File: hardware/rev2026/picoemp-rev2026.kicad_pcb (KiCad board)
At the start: 2 copper layers, 40 x 130 mm, 53 parts, among them J1 EDGE-SMA, J2 1x2_Pin_Header, J3 MKDS 1,5/2-5.08, J4 EDGE-SMA, P1 Header 7, P2 Header 2, P3 Header 4, Q1 LDA111STR, Q2 RGT16BM65DTL, Q3 AO3422, Q4 AO3422, SW1 KSC741J LFS, SW2 KSC741J LFS, SW3 TL3301AF160QJ, T1 ATB322524, T2 ATB322524, U1 SC0915, U2 74LVC1G17

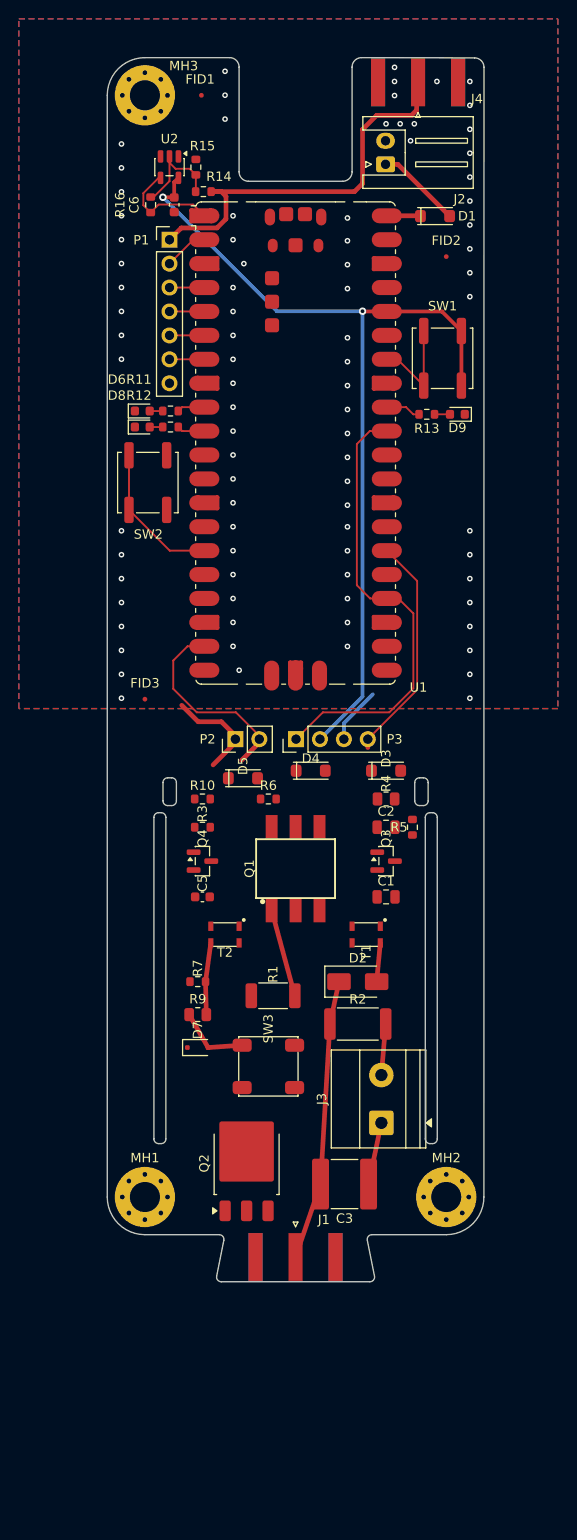
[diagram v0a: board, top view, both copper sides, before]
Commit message: Pull the barrier-limited HV tracks back to 1.150 mm
All five ended on a transformer secondary pad, whose centre sits 1.770 mm from
the primary pad centre of the same package. A 0.5 mm track centred there lands
1.020 mm from the primary pad edge -- passing the 1.000 mm barrier in CAD, but
leaving 0.020 mm for etch tolerance. Standard trace-width tolerance is around
+/-20%, which on a 0.5 mm track is +/-0.05 mm per edge, so the barrier could be
violated in production while passing in the file.

Moved those endpoints 0.130 mm further from the primary row. They stay well
inside the secondary pad (0.370 mm from its far edge), so connectivity is
untouched -- verified beforehand that exactly five segments and no vias reach
those four points.

One needed 0.145 mm rather than 0.130: /HV_RTN leaving T1.3 runs west while T1.4
sits directly above its start, so moving only one end left the segment sloped and
its closest approach, at the pad's west edge, came out at 1.141 mm.

Tightest HV-to-foreign clearance is now 1.150 mm at the transformers, up from
1.020. DRC still 0 errors, 0 warnings, 0 unconnected, parity clean.

Not touched: /HV_GATE runs 1.060 mm from MH1's pad in two places. That was not
in the five, it has three times the margin, and the track is a long vertical
with shared endpoints so pulling it cascades. Worth noting MH1's pad is floating
copper -- unconnected -- sitting beside a 250 V node.

Co-Authored-By: Claude Opus 5 <noreply@anthropic.com>
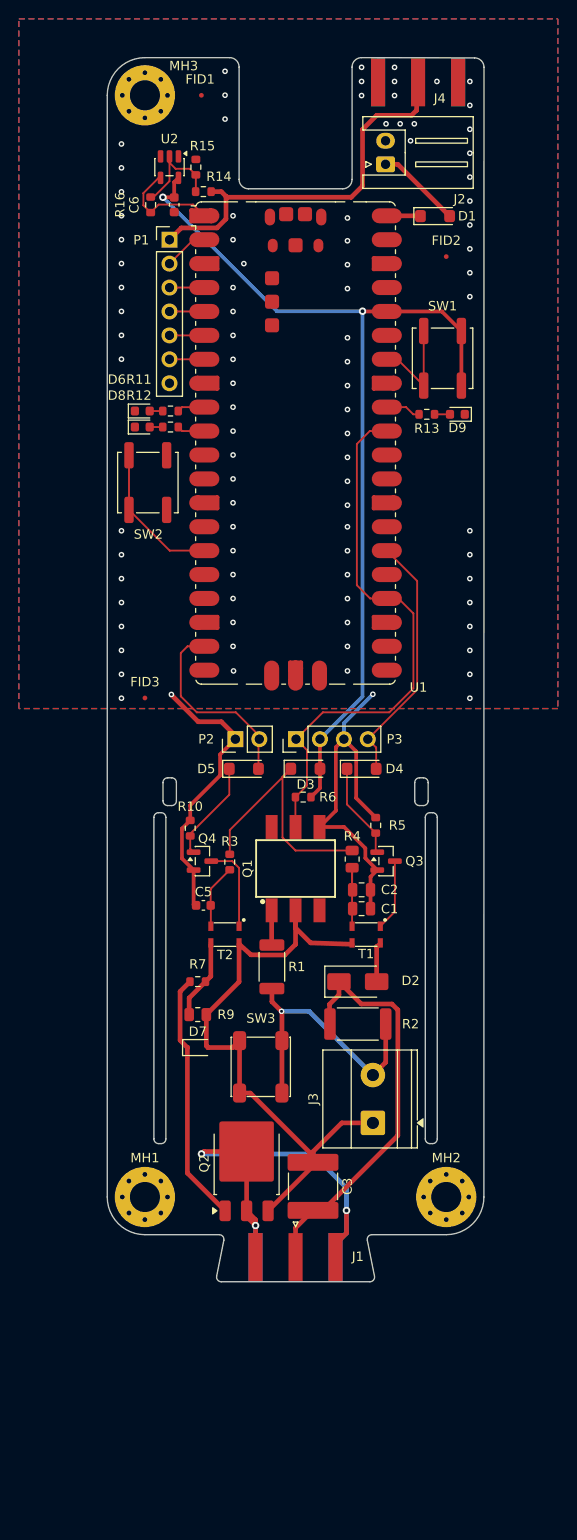
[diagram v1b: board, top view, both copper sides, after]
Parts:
- moved D3 8.57 mm to (125.4, 95.4)
- moved R4 7.33 mm to (130.4, 105.0), turned to 90 degrees
- moved C2 7.14 mm to (131.4, 108.2), turned to 180 degrees
- moved D4 5.40 mm to (131.4, 95.4)
- moved R3 4.70 mm to (117.4, 105.3), turned to 90 degrees
- moved R5 3.91 mm to (132.9, 101.4), turned to -90 degrees
- moved R6 3.71 mm to (125.2, 98.4)
- moved R10 3.36 mm to (113.2, 101.7), turned to -90 degrees
- moved C3 3.35 mm to (126.2, 139.7), turned to -90 degrees
- moved R1 3.08 mm to (121.9, 116.4), turned to 90 degrees
- moved C1 2.88 mm to (131.4, 110.2), turned to 180 degrees
- moved D5 1.00 mm to (118.9, 95.4)
- moved C5 0.91 mm to (114.6, 109.9)
- moved J3 0.90 mm to (132.6, 133.0)
- moved SW3 0.81 mm to (120.7, 127.0), turned to 90 degrees
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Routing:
- net /HV_RTN: track 14.3 -> 66.5 mm
- net /HV_OUT: track 0.00 -> 51.9 mm, vias 0 -> 3
- net GND: track 17.5 -> 69.1 mm, vias 85 -> 91
- net /PRI_CLAMP: track 0.00 -> 27.4 mm
- net /HV_GATE: track 0.00 -> 26.8 mm
- net /HV_SENSE: track 5.44 -> 30.9 mm, vias 0 -> 1
- net /HV_RAIL: track 29.8 -> 43.8 mm
- net /Q4_GATE: track 0.00 -> 10.7 mm
- net /CHARGED: track 48.6 -> 59.0 mm
- net /Q3_GATE: track 0.00 -> 10.2 mm
- net /T2_PRI_A: track 0.00 -> 9.65 mm
- net /T1_PRI_B: track 0.00 -> 8.02 mm
- net /T1_PRI_A: track 0.00 -> 7.56 mm
- net /T2_PRI_B: track 0.00 -> 6.84 mm
- net +3V3: track 94.2 -> 100.7 mm
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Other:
- outline, holes or cut-outs redrawn
- board text added: "+3V3"
- board text added: "CHARGED"
- board text added: "GND"
- board text added: "GP1"
- board text added: "GP2"
- board text added: "GP3"
- board text added: "GP4"
- board text added: "GP5"
- board text added: "HVPULSE"
- board text added: "HVPWM"
- board text added: "TRIG"
- board text removed: "1=TRIG"
- board text removed: "2-6=GPI*"
- board text removed: "7=GND"

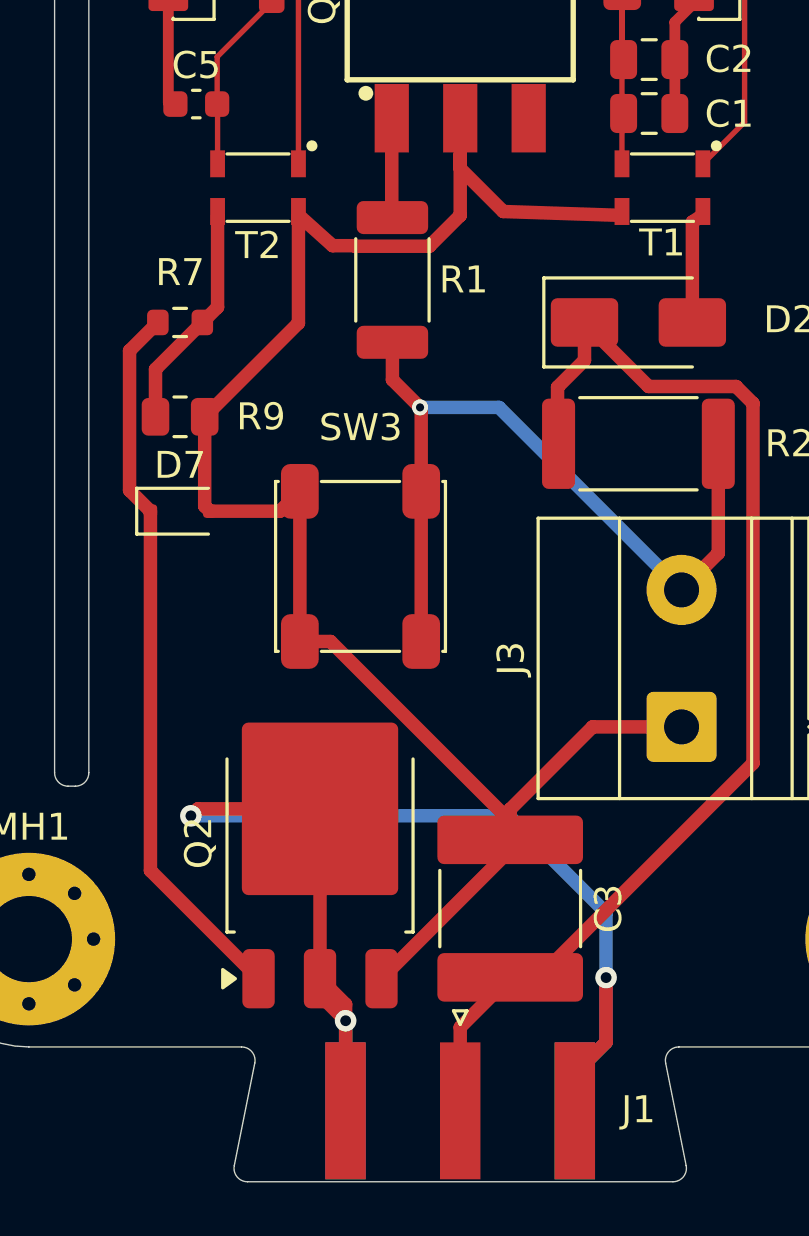
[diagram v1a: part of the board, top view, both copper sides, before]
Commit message: J4 is populated, not DNP
The schematic now marks J4 as fitted and the board footprint agrees, so the test
asserting DNP was failing. Updated to assert the opposite, with a note on why it
matters beyond the BOM: J4 got the cramped east strip precisely because it was
optional and the USB notch was not. That trade no longer holds the same way.

R16 remains the only DNP part, which is correct -- it is the 0R bypass across
the trigger buffer.

Co-Authored-By: Claude Opus 5 <noreply@anthropic.com>
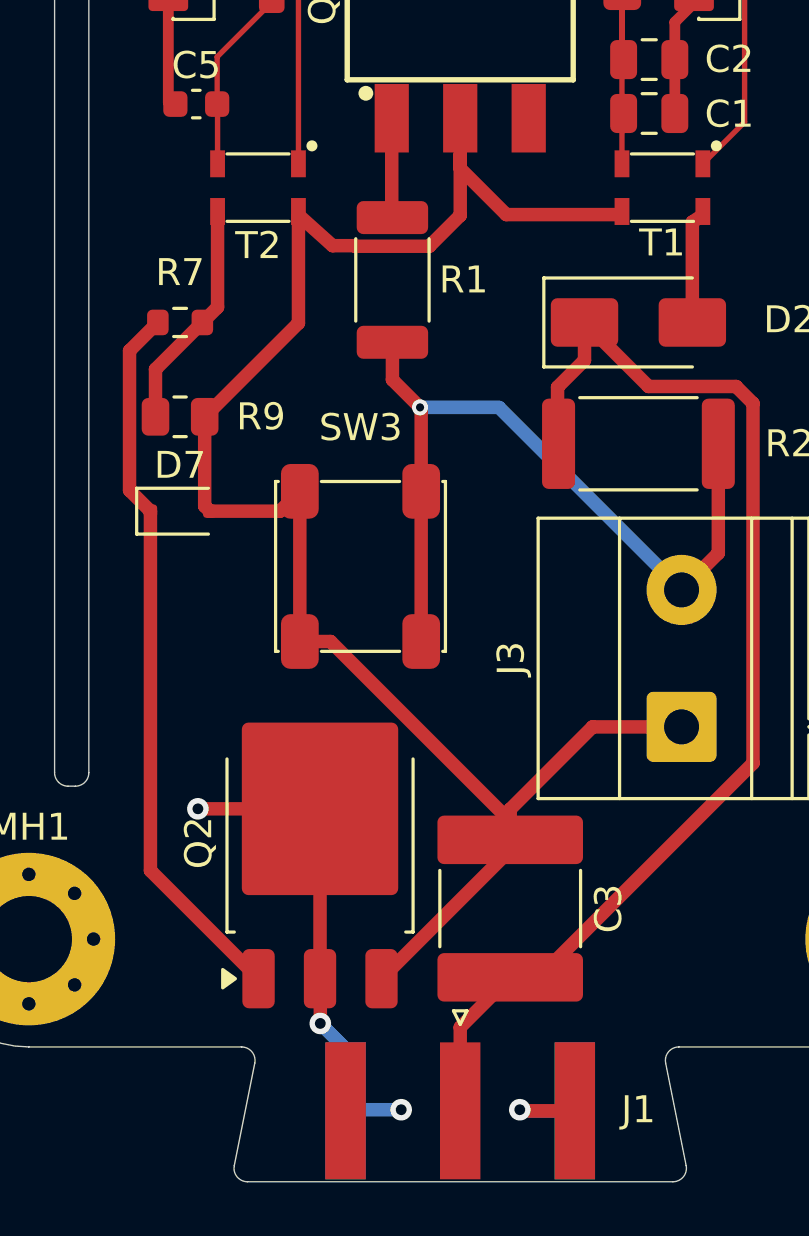
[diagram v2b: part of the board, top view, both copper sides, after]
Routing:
- net /HV_OUT: track 51.9 -> 22.3 mm, vias 3 -> 4

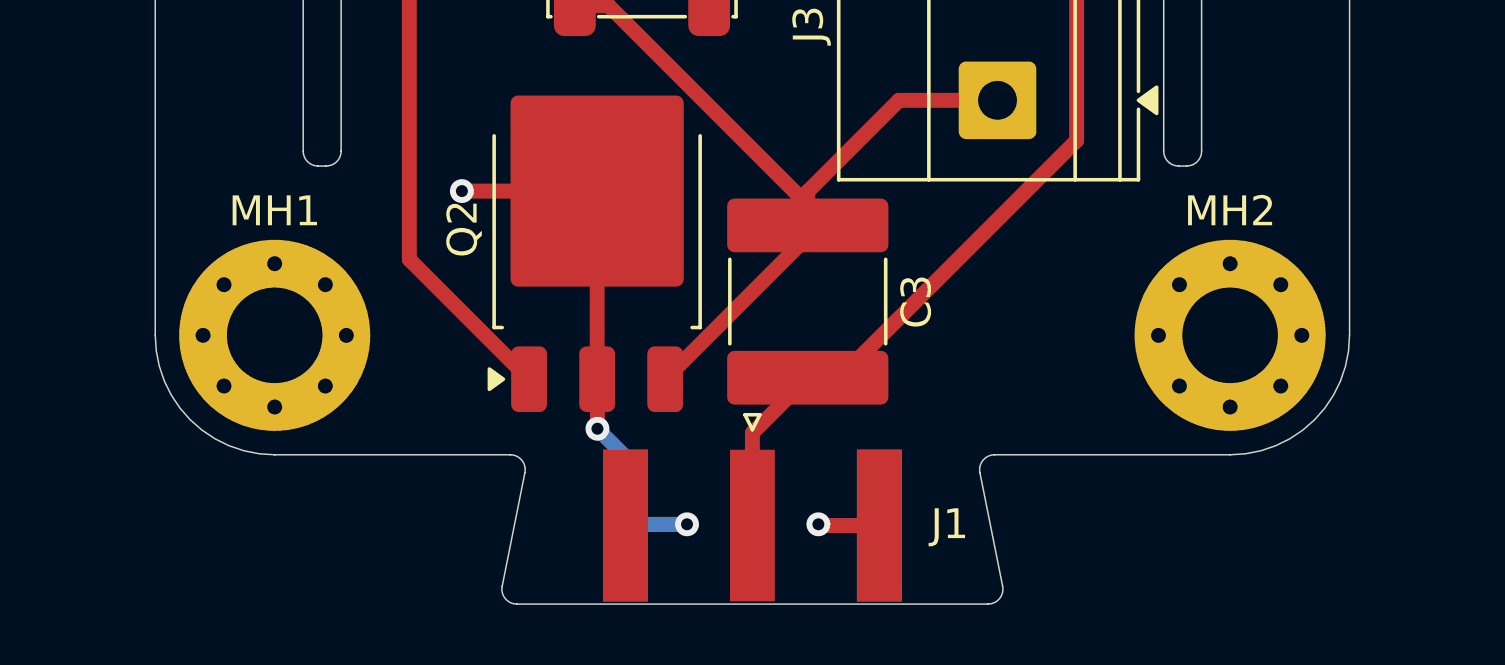
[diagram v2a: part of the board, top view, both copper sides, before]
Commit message: MH1/MH2 to bare non-plated holes; HV_OUT reroute
MH1 and MH2 are now MountingHole_3.2mm_M3 as np_thru_hole -- no copper at all.
That removes two 6.4 mm floating pads from beside a 250 V node, and with them the
tightest barrier gap on the board: /HV_GATE was running 1.060 mm from MH1's pad.
The limit is now the transformers again at 1.135 mm. MH3 keeps its plated pad;
it sits at the logic end where floating copper is not a concern.

HV_OUT rerouted: 51.9 -> 22.2 mm. Discharge loop total 162.5 -> 131.5 mm.

Still open: one dangling via at (122.20, 147.20), B.Cu only, and J1's left shield
tab at (120.14, 147.2417) is not connected to copper. Electrically the shield is
one piece through the connector body, but DRC counts the islands.

Co-Authored-By: Claude Opus 5 <noreply@anthropic.com>
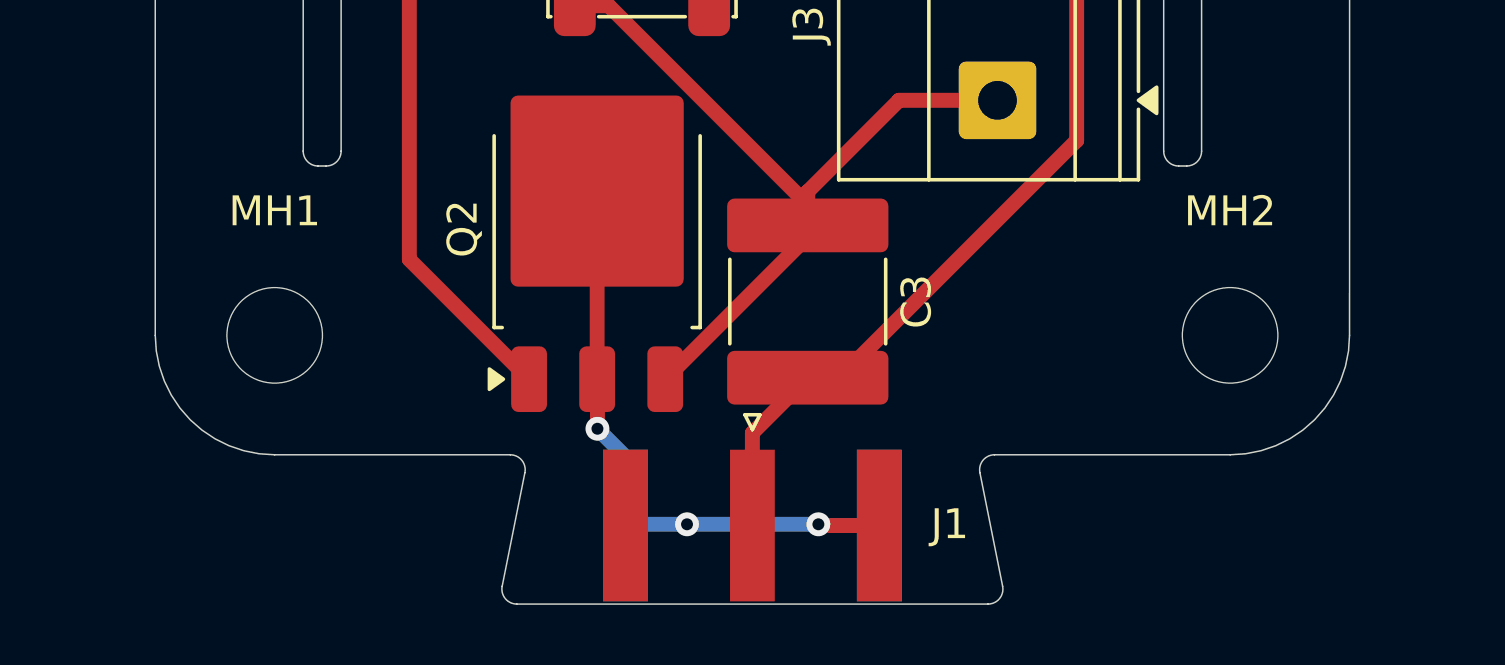
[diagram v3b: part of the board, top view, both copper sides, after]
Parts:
- MH1, MH2: footprint MountingHole:MountingHole_3.2mm_M3_Pad_Via -> MountingHole:MountingHole_3.2mm_M3
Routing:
- net /HV_RAIL: track 43.8 -> 42.7 mm
- net /HV_OUT: track 22.3 -> 22.2 mm, vias 4 -> 3
